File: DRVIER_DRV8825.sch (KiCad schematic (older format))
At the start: 23 parts, among them P7 CONN_01X05, P8 CONN_01X03, P9 CONN_02X08, U5 DRV8825

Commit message: some modifications, before creating an array
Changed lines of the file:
@@
 $Descr A4 11693 8268
 encoding utf-8
-Sheet 2 5
+Sheet 4 5
 Title ""
 Date ""
@@
 AR Path="/56024A8C/560152AD" Ref="U7"  Part="1"
 AR Path="/56024B67/560152AD" Ref="U8"  Part="1"
-F 0 "U8" H 5850 3800 50  0000 C CNN
+F 0 "U7" H 5850 3800 50  0000 C CNN
 F 1 "DRV8825" H 5850 4000 50  0000 C CNN
 F 2 "libs:drv8825" H 5850 3900 50  0001 C CNN
@@
 AR Path="/56024A8C/560153B8" Ref="P15"  Part="1"
 AR Path="/56024B67/560153B8" Ref="P18"  Part="1"
-F 0 "P18" H 8800 4000 50  0000 C CNN
+F 0 "P15" H 8800 4000 50  0000 C CNN
 F 1 "CONN_02X08" V 8800 3550 50  0000 C CNN
 F 2 "libs:SW_DIP_x8_Slide_changed_numbering" H 8800 2350 60  0000 C CNN
@@
 AR Path="/56024A8C/56015588" Ref="R46"  Part="1"
 AR Path="/56024B67/56015588" Ref="R58"  Part="1"
-F 0 "R58" V 7330 4250 50  0000 C CNN
+F 0 "R46" V 7330 4250 50  0000 C CNN
 F 1 "10k" V 7250 4250 50  0000 C CNN
 F 2 "Resistors_SMD:R_1206_HandSoldering" V 7180 4250 30  0000 C CNN
@@
 AR Path="/56024A8C/56015719" Ref="C27"  Part="1"
 AR Path="/56024B67/56015719" Ref="C32"  Part="1"
-F 0 "C32" H 6775 4800 50  0000 L CNN
+F 0 "C27" H 6775 4800 50  0000 L CNN
 F 1 "0.47u" H 6775 4600 50  0000 L CNN
 F 2 "Capacitors_SMD:C_1206_HandSoldering" H 6788 4550 30  0000 C CNN
@@
 AR Path="/56024A8C/560158A5" Ref="#PWR053"  Part="1"
 AR Path="/56024B67/560158A5" Ref="#PWR063"  Part="1"
-F 0 "#PWR063" H 7000 3000 50  0001 C CNN
+F 0 "#PWR053" H 7000 3000 50  0001 C CNN
 F 1 "Earth" H 7000 3100 50  0001 C CNN
 F 2 "" H 7000 3250 60  0000 C CNN
@@
 AR Path="/56024A8C/56015D77" Ref="#PWR054"  Part="1"
 AR Path="/56024B67/56015D77" Ref="#PWR064"  Part="1"
-F 0 "#PWR064" H 6750 4750 50  0001 C CNN
+F 0 "#PWR054" H 6750 4750 50  0001 C CNN
 F 1 "Earth" H 6750 4850 50  0001 C CNN
 F 2 "" H 6750 5000 60  0000 C CNN
@@
 AR Path="/56024A8C/56016C3E" Ref="R53"  Part="1"
 AR Path="/56024B67/56016C3E" Ref="R65"  Part="1"
-F 0 "R65" V 8280 3050 50  0000 C CNN
+F 0 "R53" V 8280 3050 50  0000 C CNN
 F 1 "10k" V 8200 3050 50  0000 C CNN
 F 2 "Resistors_SMD:R_1206_HandSoldering" V 8130 3050 30  0000 C CNN
@@
 AR Path="/56024A8C/5601705B" Ref="R52"  Part="1"
 AR Path="/56024B67/5601705B" Ref="R64"  Part="1"
-F 0 "R64" V 8130 3050 50  0000 C CNN
+F 0 "R52" V 8130 3050 50  0000 C CNN
 F 1 "10k" V 8050 3050 50  0000 C CNN
 F 2 "Resistors_SMD:R_1206_HandSoldering" V 7980 3050 30  0000 C CNN
@@
 AR Path="/56024A8C/560170AC" Ref="R51"  Part="1"
 AR Path="/56024B67/560170AC" Ref="R63"  Part="1"
-F 0 "R63" V 7980 3050 50  0000 C CNN
+F 0 "R51" V 7980 3050 50  0000 C CNN
 F 1 "10k" V 7900 3050 50  0000 C CNN
 F 2 "Resistors_SMD:R_1206_HandSoldering" V 7830 3050 30  0000 C CNN
@@
 AR Path="/56024A8C/560170E0" Ref="R50"  Part="1"
 AR Path="/56024B67/560170E0" Ref="R62"  Part="1"
-F 0 "R62" V 7830 3050 50  0000 C CNN
+F 0 "R50" V 7830 3050 50  0000 C CNN
 F 1 "10k" V 7750 3050 50  0000 C CNN
 F 2 "Resistors_SMD:R_1206_HandSoldering" V 7680 3050 30  0000 C CNN
@@
 AR Path="/56024A8C/56017121" Ref="R49"  Part="1"
 AR Path="/56024B67/56017121" Ref="R61"  Part="1"
-F 0 "R61" V 7680 3050 50  0000 C CNN
+F 0 "R49" V 7680 3050 50  0000 C CNN
 F 1 "10k" V 7600 3050 50  0000 C CNN
 F 2 "Resistors_SMD:R_1206_HandSoldering" V 7530 3050 30  0000 C CNN
@@
 AR Path="/56024A8C/5601715F" Ref="R48"  Part="1"
 AR Path="/56024B67/5601715F" Ref="R60"  Part="1"
-F 0 "R60" V 7530 3050 50  0000 C CNN
+F 0 "R48" V 7530 3050 50  0000 C CNN
 F 1 "10k" V 7450 3050 50  0000 C CNN
 F 2 "Resistors_SMD:R_1206_HandSoldering" V 7380 3050 30  0000 C CNN
@@
 AR Path="/56024A8C/560171A0" Ref="R47"  Part="1"
 AR Path="/56024B67/560171A0" Ref="R59"  Part="1"
-F 0 "R59" V 7380 3050 50  0000 C CNN
+F 0 "R47" V 7380 3050 50  0000 C CNN
 F 1 "10k" V 7300 3050 50  0000 C CNN
 F 2 "Resistors_SMD:R_1206_HandSoldering" V 7230 3050 30  0000 C CNN
@@
 AR Path="/56024A8C/560171FA" Ref="R45"  Part="1"
 AR Path="/56024B67/560171FA" Ref="R57"  Part="1"
-F 0 "R57" V 7230 3050 50  0000 C CNN
+F 0 "R45" V 7230 3050 50  0000 C CNN
 F 1 "10k" V 7150 3050 50  0000 C CNN
 F 2 "Resistors_SMD:R_1206_HandSoldering" V 7080 3050 30  0000 C CNN
@@
 AR Path="/56024A8C/56019940" Ref="P14"  Part="1"
 AR Path="/56024B67/56019940" Ref="P17"  Part="1"
-F 0 "P17" H 3700 4550 50  0000 C CNN
+F 0 "P14" H 3700 4550 50  0000 C CNN
 F 1 "CONN_01X03" V 3800 4350 50  0000 C CNN
 F 2 "Pin_Headers:Pin_Header_Straight_1x03" H 3700 4350 60  0001 C CNN
@@
 AR Path="/56024A8C/56019B0B" Ref="#PWR055"  Part="1"
 AR Path="/56024B67/56019B0B" Ref="#PWR065"  Part="1"
-F 0 "#PWR065" H 9350 3300 50  0001 C CNN
+F 0 "#PWR055" H 9350 3300 50  0001 C CNN
 F 1 "Earth" H 9350 3400 50  0001 C CNN
 F 2 "" H 9350 3550 60  0000 C CNN
@@
 AR Path="/56024A8C/5601A093" Ref="#PWR056"  Part="1"
 AR Path="/56024B67/5601A093" Ref="#PWR066"  Part="1"
-F 0 "#PWR066" H 4950 4300 50  0001 C CNN
+F 0 "#PWR056" H 4950 4300 50  0001 C CNN
 F 1 "Earth" H 4950 4400 50  0001 C CNN
 F 2 "" H 4950 4550 60  0000 C CNN
@@
 AR Path="/56024A8C/5601A7DF" Ref="RV3"  Part="1"
 AR Path="/56024B67/5601A7DF" Ref="RV4"  Part="1"
-F 0 "RV4" H 4350 4700 50  0000 C CNN
+F 0 "RV3" H 4350 4700 50  0000 C CNN
 F 1 "POT" H 4350 4800 50  0000 C CNN
 F 2 "Potentiometers:Potentiometer_Bourns_3296P_3-8Zoll_Angular_ScrewFront" H 4350 4800 60  0001 C CNN
@@
 AR Path="/56024A8C/5601AA2D" Ref="#PWR057"  Part="1"
 AR Path="/56024B67/5601AA2D" Ref="#PWR067"  Part="1"
-F 0 "#PWR067" H 4750 4550 50  0001 C CNN
+F 0 "#PWR057" H 4750 4550 50  0001 C CNN
 F 1 "Earth" H 4750 4650 50  0001 C CNN
 F 2 "" H 4750 4800 60  0000 C CNN
@@
 AR Path="/56024A8C/5601AF31" Ref="#PWR058"  Part="1"
 AR Path="/56024B67/5601AF31" Ref="#PWR068"  Part="1"
-F 0 "#PWR068" H 7900 2400 50  0001 C CNN
+F 0 "#PWR058" H 7900 2400 50  0001 C CNN
 F 1 "+3.3V" H 7900 2690 50  0000 C CNN
 F 2 "" H 7900 2550 60  0000 C CNN
@@
 AR Path="/56024A8C/5601B289" Ref="#PWR059"  Part="1"
 AR Path="/56024B67/5601B289" Ref="#PWR069"  Part="1"
-F 0 "#PWR069" H 4000 4650 50  0001 C CNN
+F 0 "#PWR059" H 4000 4650 50  0001 C CNN
 F 1 "+3.3V" H 4000 4940 50  0000 C CNN
 F 2 "" H 4000 4800 60  0000 C CNN
@@
 AR Path="/56024A8C/5601C076" Ref="R44"  Part="1"
 AR Path="/56024B67/5601C076" Ref="R56"  Part="1"
-F 0 "R56" V 4930 4050 50  0000 C CNN
+F 0 "R44" V 4930 4050 50  0000 C CNN
 F 1 "200m" V 4850 4050 50  0000 C CNN
 F 2 "Resistors_ThroughHole:Resistor_Horizontal_RM15mm" V 4780 4050 30  0001 C CNN
@@
 AR Path="/56024A8C/5601C0DF" Ref="R43"  Part="1"
 AR Path="/56024B67/5601C0DF" Ref="R55"  Part="1"
-F 0 "R55" V 4930 3750 50  0000 C CNN
+F 0 "R43" V 4930 3750 50  0000 C CNN
 F 1 "200m" V 4850 3750 50  0000 C CNN
 F 2 "Resistors_ThroughHole:Resistor_Horizontal_RM15mm" V 4780 3750 30  0001 C CNN
@@
 AR Path="/56024A8C/5601CB84" Ref="C24"  Part="1"
 AR Path="/56024B67/5601CB84" Ref="C29"  Part="1"
-F 0 "C29" H 4475 3800 50  0000 L CNN
+F 0 "C24" H 4475 3800 50  0000 L CNN
 F 1 "0.1u" H 4475 3600 50  0000 L CNN
 F 2 "Capacitors_SMD:C_1206_HandSoldering" H 4488 3550 30  0000 C CNN
@@
 AR Path="/56024A8C/5601CDD0" Ref="C25"  Part="1"
 AR Path="/56024B67/5601CDD0" Ref="C30"  Part="1"
-F 0 "C30" H 4475 4200 50  0000 L CNN
+F 0 "C25" H 4475 4200 50  0000 L CNN
 F 1 "0.1u" H 4475 4000 50  0000 L CNN
 F 2 "Capacitors_SMD:C_1206_HandSoldering" H 4488 3950 30  0000 C CNN
@@
 AR Path="/56024A8C/5601D03F" Ref="#PWR060"  Part="1"
 AR Path="/56024B67/5601D03F" Ref="#PWR070"  Part="1"
-F 0 "#PWR070" H 4650 3500 50  0001 C CNN
+F 0 "#PWR060" H 4650 3500 50  0001 C CNN
 F 1 "Earth" H 4650 3600 50  0001 C CNN
 F 2 "" H 4650 3750 60  0000 C CNN
@@
 AR Path="/56024A8C/5601D141" Ref="#PWR061"  Part="1"
 AR Path="/56024B67/5601D141" Ref="#PWR071"  Part="1"
-F 0 "#PWR071" H 4650 3800 50  0001 C CNN
+F 0 "#PWR061" H 4650 3800 50  0001 C CNN
 F 1 "Earth" H 4650 3900 50  0001 C CNN
 F 2 "" H 4650 4050 60  0000 C CNN
@@
 AR Path="/56024A8C/5601DA97" Ref="#PWR062"  Part="1"
 AR Path="/56024B67/5601DA97" Ref="#PWR072"  Part="1"
-F 0 "#PWR072" H 4400 3650 50  0001 C CNN
+F 0 "#PWR062" H 4400 3650 50  0001 C CNN
 F 1 "Earth" H 4400 3750 50  0001 C CNN
 F 2 "" H 4400 3900 60  0000 C CNN
@@
 AR Path="/56024A8C/5601EA8E" Ref="R42"  Part="1"
 AR Path="/56024B67/5601EA8E" Ref="R54"  Part="1"
-F 0 "R54" V 4630 3350 50  0000 C CNN
+F 0 "R42" V 4630 3350 50  0000 C CNN
 F 1 "1M" V 4550 3350 50  0000 C CNN
 F 2 "Resistors_SMD:R_1206_HandSoldering" V 4480 3350 30  0000 C CNN
@@
 AR Path="/56024A8C/5601ED30" Ref="C23"  Part="1"
 AR Path="/56024B67/5601ED30" Ref="C28"  Part="1"
-F 0 "C28" H 4425 3450 50  0000 L CNN
+F 0 "C23" H 4425 3450 50  0000 L CNN
 F 1 "0.1u" H 4425 3250 50  0000 L CNN
 F 2 "Capacitors_SMD:C_1206_HandSoldering" H 4438 3200 30  0000 C CNN
@@
 AR Path="/56024A8C/5601F244" Ref="C26"  Part="1"
 AR Path="/56024B67/5601F244" Ref="C31"  Part="1"
-F 0 "C31" H 4975 3350 50  0000 L CNN
+F 0 "C26" H 4975 3350 50  0000 L CNN
 F 1 "0.01u" H 4975 3150 50  0000 L CNN
 F 2 "Capacitors_SMD:C_1206_HandSoldering" H 4988 3100 30  0000 C CNN
@@
 AR Path="/56024A8C/56021497" Ref="D4"  Part="1"
 AR Path="/56024B67/56021497" Ref="D5"  Part="1"
-F 0 "D5" H 7650 4350 50  0000 C CNN
+F 0 "D4" H 7650 4350 50  0000 C CNN
 F 1 "LED" H 7650 4150 50  0000 C CNN
 F 2 "LEDs:LED-5MM" H 7650 4250 60  0001 C CNN
@@
 Wire Wire Line
 	7850 4250 8200 4250
-Text Label 7900 4250 0    60   ~ 0
-3.3Vlocal
 Wire Wire Line
 	7450 4250 7400 4250
@@
 AR Path="/56024A8C/5606EDF9" Ref="P13"  Part="1"
 AR Path="/56024B67/5606EDF9" Ref="P16"  Part="1"
-F 0 "P16" H 3250 3550 50  0000 C CNN
+F 0 "P13" H 3250 3550 50  0000 C CNN
 F 1 "CONN_01X05" V 3350 3250 50  0000 C CNN
 F 2 "libs:PIN_1x5_0.2inch" H 3250 3250 60  0000 C CNN
@@
 	-1   0    0    1
 $EndComp
+$Comp
+L +3.3V #PWR?
+U 1 1 560D5DEA
+P 8200 4250
+F 0 "#PWR?" H 8200 4100 50  0001 C CNN
+F 1 "+3.3V" H 8200 4390 50  0000 C CNN
+F 2 "" H 8200 4250 60  0000 C CNN
+F 3 "" H 8200 4250 60  0000 C CNN
+	1    8200 4250
+	1    0    0    -1
+$EndComp
 $EndSCHEMATC

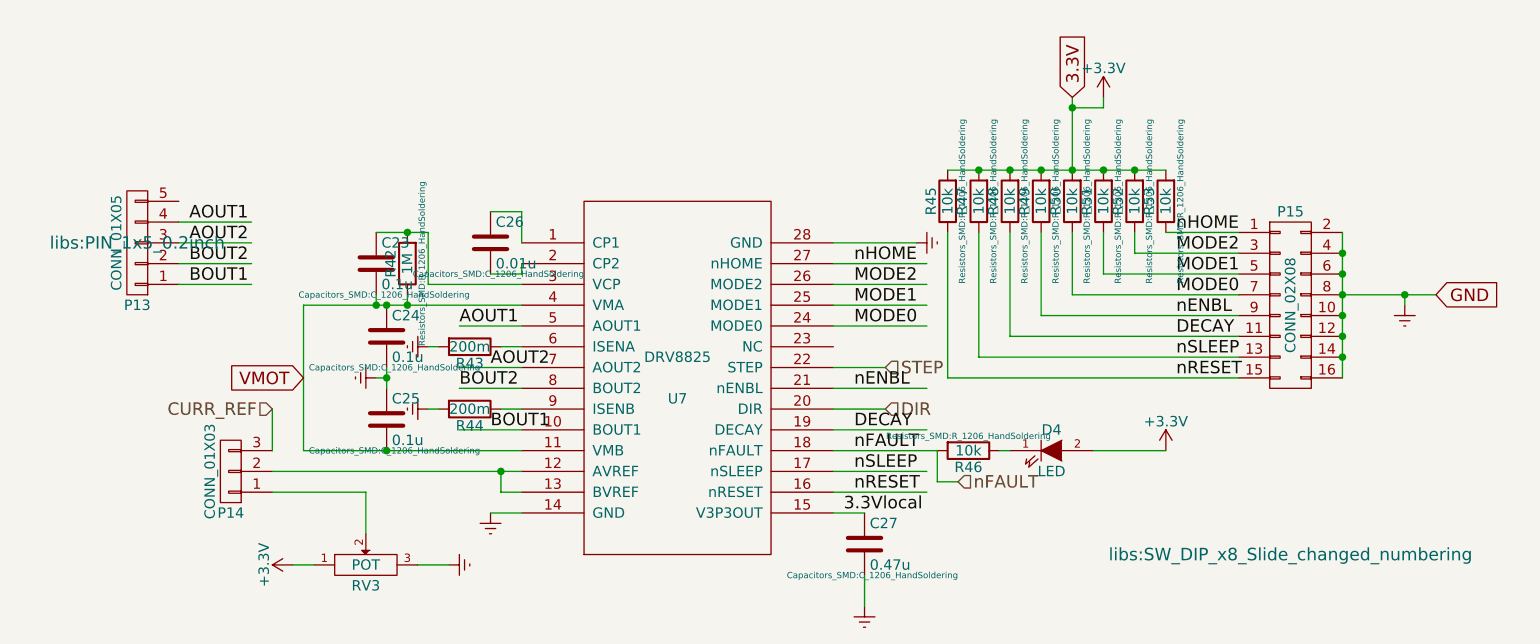
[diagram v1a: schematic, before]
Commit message: trafo bent
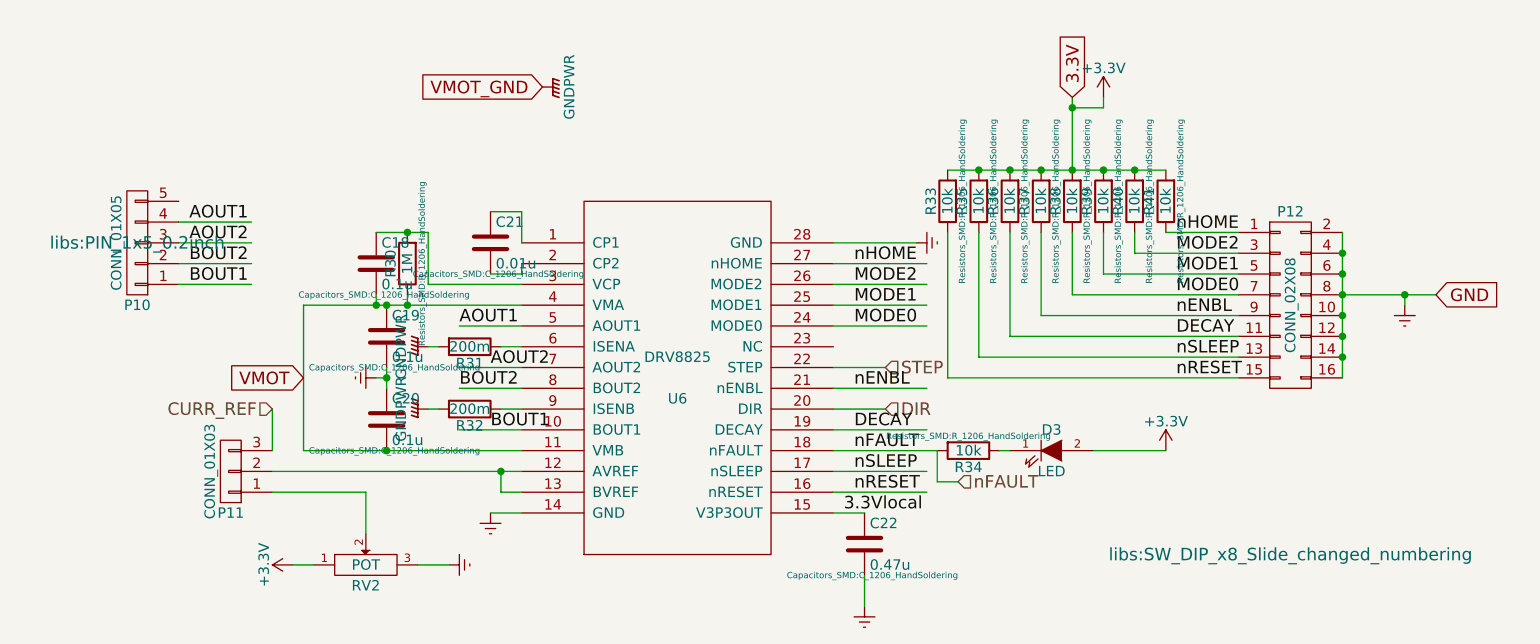
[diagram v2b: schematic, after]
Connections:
- net labels added: GNDPWR, VMOT_GND
